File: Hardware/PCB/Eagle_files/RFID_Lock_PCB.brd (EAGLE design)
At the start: 72.1 x 76.2 mm, 38 parts, among them IC1 74AHCT125, J3 Servo, K1 351, T2 2N2222

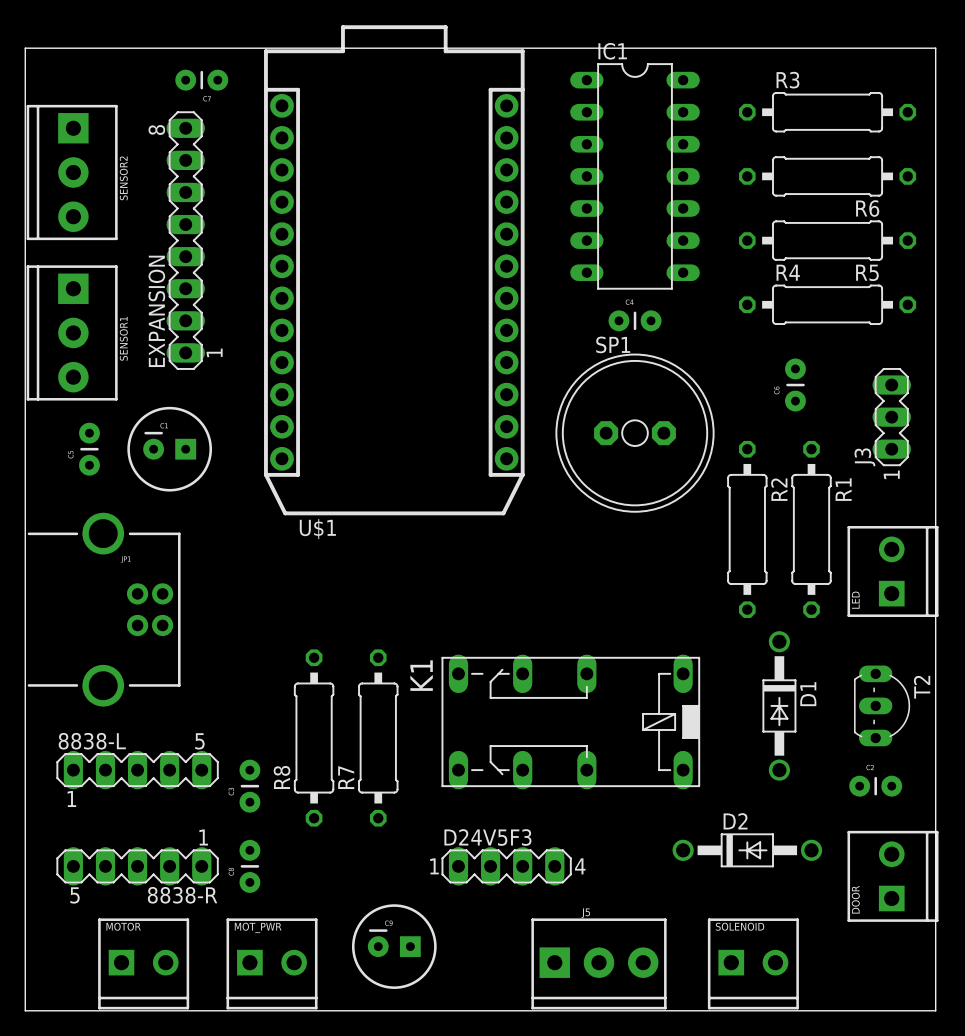
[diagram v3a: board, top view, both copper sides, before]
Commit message: Update RFID_Lock_PCB.brd
Added mounting holes to PCB
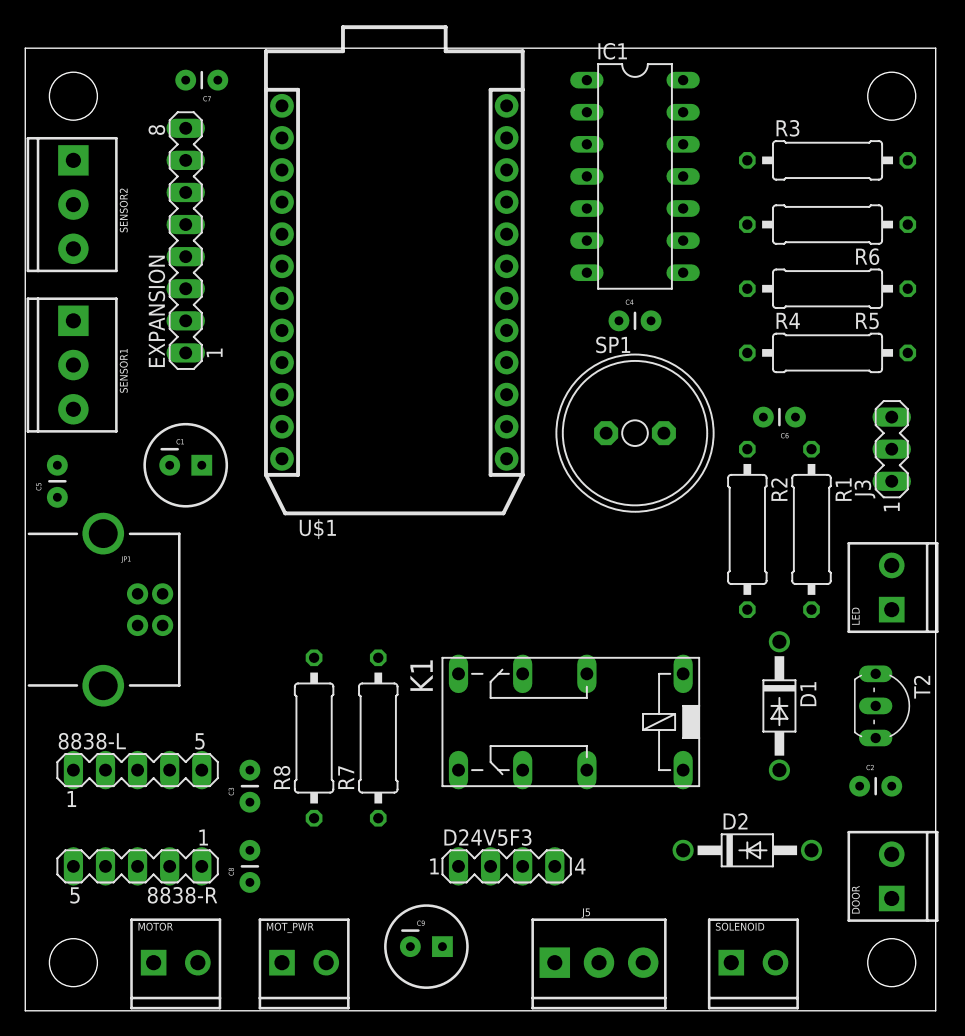
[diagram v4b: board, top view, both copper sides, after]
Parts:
- moved R6 3.81 mm to (63.5, 62.2)
- moved R3 3.81 mm to (63.5, 67.3)
- moved R4 3.81 mm to (63.5, 52.1)
- moved R5 3.81 mm to (63.5, 57.1)
- moved C5 3.59 mm to (2.54, 40.6)
- moved MOTOR 2.54 mm to (10.2, 3.81)
- moved C9 2.54 mm to (31.8, 5.08)
- moved J3 2.54 mm to (68.6, 44.5)
- moved MOT_PWR 2.54 mm to (20.3, 3.81)
- moved SENSOR1 2.54 mm to (3.81, 54.6)
- moved SENSOR2 2.54 mm to (3.81, 67.3)
- moved C1 1.80 mm to (12.7, 43.2)
- moved LED 1.27 mm to (68.6, 31.8)
- moved C6 1.27 mm to (61.0, 47.0), turned to 180 degrees

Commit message: Update RFID_Lock_PCB.brd
Autorouted and copper poured the .brd file.  Passes DRC.
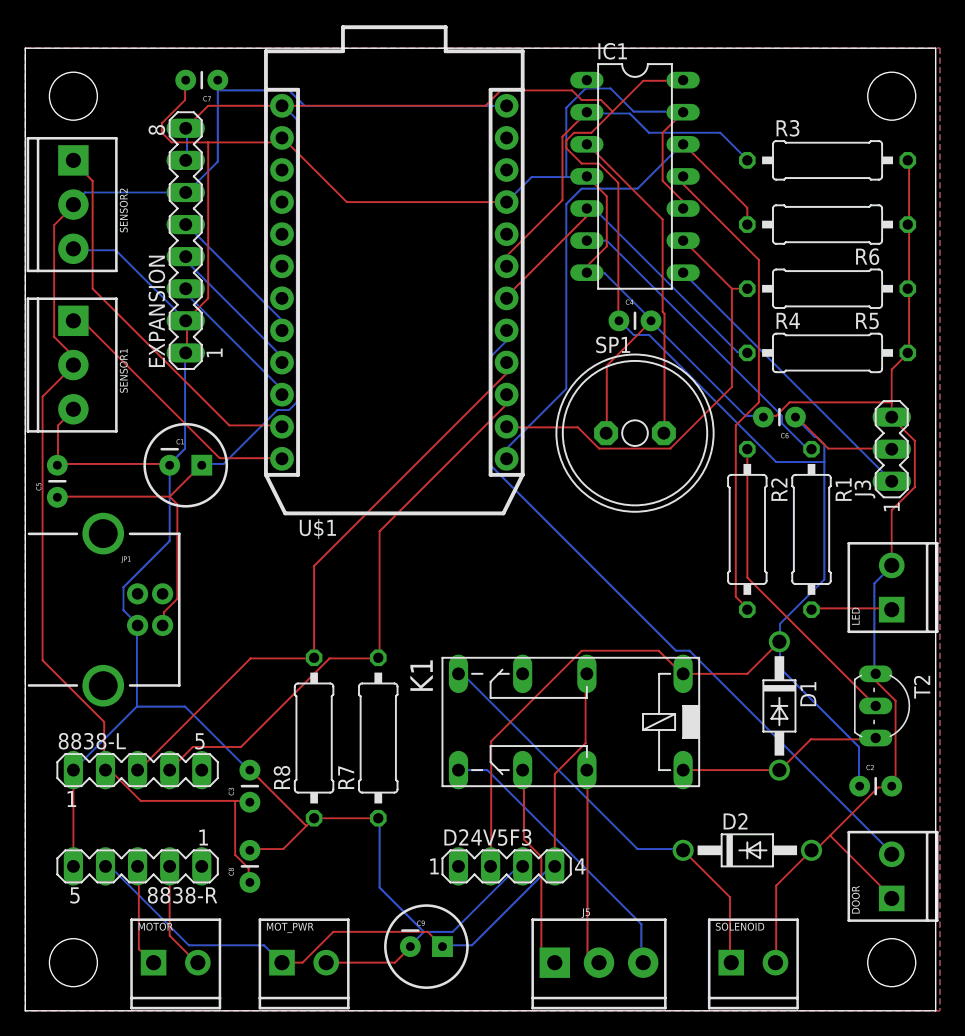
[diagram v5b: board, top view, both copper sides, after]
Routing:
- net GND: track 0.00 -> 341.4 mm
- net VCC: track 0.00 -> 225.0 mm
- net +3.3V: track 0.00 -> 111.3 mm
- net N$6: track 0.00 -> 59.2 mm
- net N$11: track 0.00 -> 55.7 mm
- net N$5: track 0.00 -> 47.4 mm
- net N$12: track 0.00 -> 45.2 mm
- net N$17: track 0.00 -> 41.8 mm
- net N$19: track 0.00 -> 37.9 mm
- net N$7: track 0.00 -> 35.0 mm
- net N$22: track 0.00 -> 34.1 mm
- net N$2: track 0.00 -> 30.3 mm
- net N$4: track 0.00 -> 29.2 mm
- net N$23: track 0.00 -> 27.2 mm
- net N$14: track 0.00 -> 25.5 mm
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- added copper zone on layer 1, net GND
- added copper zone on layer 16, net GND
